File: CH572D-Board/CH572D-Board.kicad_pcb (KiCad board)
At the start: 2 copper layers, 16.4 x 26.4 mm, 17 parts, among them J1 12402012E212A, J2 Conn_PinHeader_1x07_P2.54mm_V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, U2 MIC5504-3.3YM5-TR, Y1 32mhz

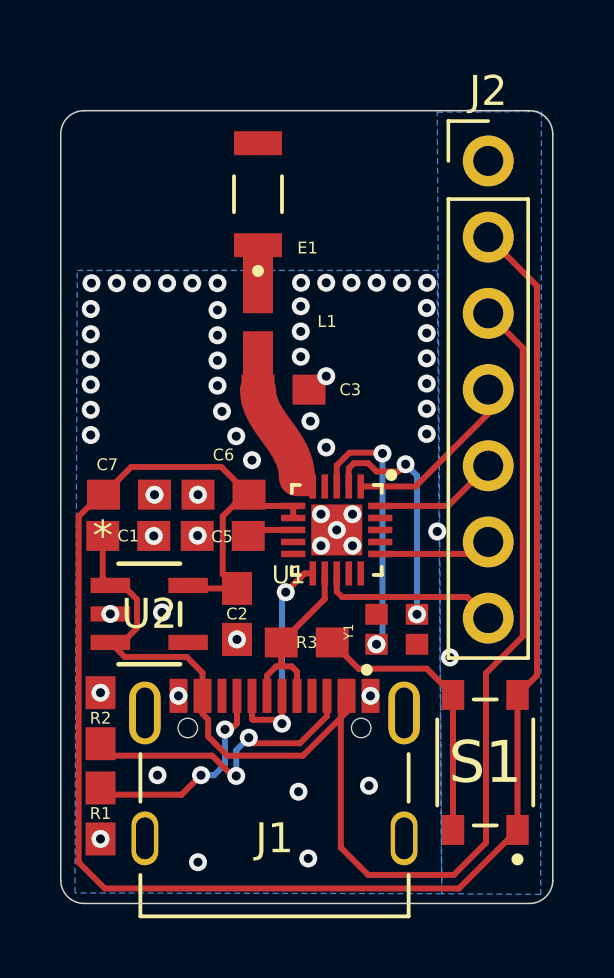
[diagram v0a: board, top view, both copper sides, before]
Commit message: fixed 5v
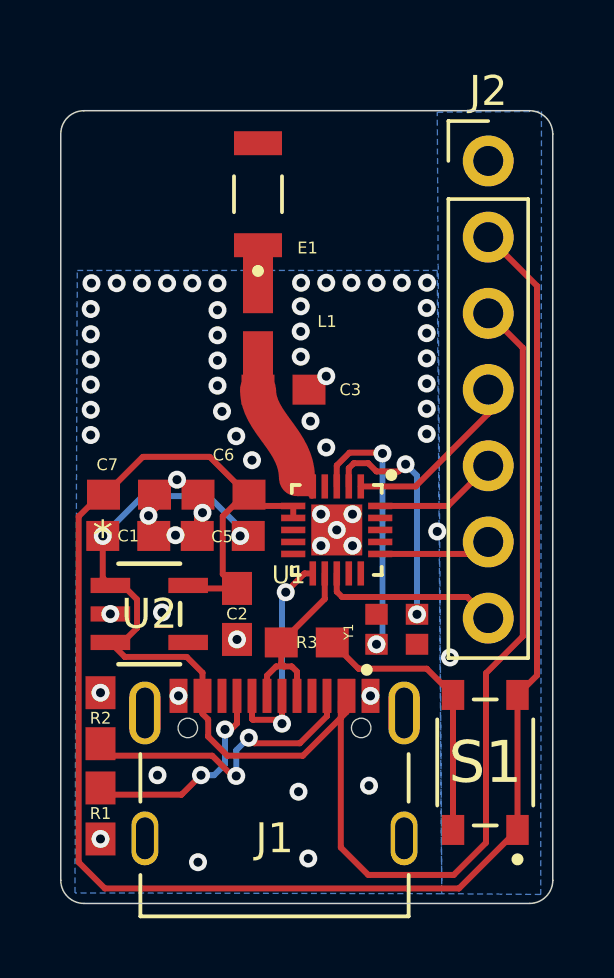
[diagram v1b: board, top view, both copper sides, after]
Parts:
- C1: value 1uF -> 0.1uF
- U2: value MIC5504-3.3YM5-TR -> the really cheap one (200mah)
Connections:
- C5 pad 1: V5 -> +5V
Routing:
- net +5V: track 46.0 -> 51.9 mm, vias 0 -> 2
- net GND: track 0.07 -> 2.55 mm
- net V5: track 1.58 -> 0.00 mm
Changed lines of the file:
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@@
 			)
 		)
-		(property "Value" "MIC5504-3.3YM5-TR"
+		(property "Value" "the really cheap one (200mah)"
 			(at 0 0 0)
 			(unlocked yes)
@@
 			(size 1.1 1)
 			(layers "F.Cu" "F.Mask" "F.Paste")
-			(net 11 "V5")
+			(net 1 "+5V")
 			(pintype "passive")
 			(solder_mask_margin 0.102)
@@
 			)
 		)
-		(property "Value" "1uF"
+		(property "Value" "0.1uF"
 			(at 1.34 1.27 0)
 			(layer "F.Fab")
@@
 		(net 1)
 	)
+	(via
+		(at 154.525 133.775)
+		(size 0.6)
+		(drill 0.3)
+		(layers "F.Cu" "B.Cu")
+		(net 1)
+	)
+	(via
+		(at 159.107 133.775)
+		(size 0.6)
+		(drill 0.3)
+		(layers "F.Cu" "B.Cu")
+		(net 1)
+	)
 	(segment
-		(start 157.6875 133.7625)
-		(end 157.675 133.775)
+		(start 155.854 132.446)
+		(end 158.046 132.446)
 		(width 0.2)
-		(layer "F.Cu")
-		(net 2)
+		(layer "B.Cu")
+		(net 1)
+	)
+	(segment
+		(start 159.107 133.507)
+		(end 159.107 133.775)
+		(width 0.2)
+		(layer "B.Cu")
+		(net 1)
+	)
+	(segment
+		(start 154.525 133.775)
+		(end 155.854 132.446)
+		(width 0.2)
+		(layer "B.Cu")
+		(net 1)
+	)
+	(segment
+		(start 158.046 132.446)
+		(end 159.107 133.507)
+		(width 0.2)
+		(layer "B.Cu")
+		(net 1)
 	)
 	(segment
 		(start 156.225 132.425)
-		(end 156.25 132.4)
+		(end 156.3 132.5)
 		(width 0.2)
 		(layer "F.Cu")
@@
 	(segment
 		(start 157.7 133.75)
-		(end 157.6875 133.7625)
+		(end 157.675002 133.725002)
+		(width 0.2)
+		(layer "F.Cu")
+		(net 2)
+	)
+	(segment
+		(start 157.75 133)
+		(end 157.85 133)
+		(width 0.2)
+		(layer "F.Cu")
+		(net 2)
+	)
+	(segment
+		(start 157.675 133.775)
+		(end 157.675 133.075)
+		(width 0.2)
+		(layer "F.Cu")
+		(net 2)
+	)
+	(segment
+		(start 157.675 133.075)
+		(end 157.75 133)
+		(width 0.2)
+		(layer "F.Cu")
+		(net 2)
+	)
+	(segment
+		(start 156.3 132.85)
+		(end 156.05 133.1)
+		(width 0.2)
+		(layer "F.Cu")
+		(net 2)
+	)
+	(segment
+		(start 157.675002 133.725002)
+		(end 157.675002 133.174998)
+		(width 0.2)
+		(layer "F.Cu")
+		(net 2)
+	)
+	(segment
+		(start 156.3 132.5)
+		(end 156.3 132.85)
+		(width 0.2)
+		(layer "F.Cu")
+		(net 2)
+	)
+	(segment
+		(start 157.675002 133.174998)
+		(end 157.85 133)
 		(width 0.2)
 		(layer "F.Cu")
@@
 	)
 	(via
-		(at 157.6875 133.7625)
+		(at 157.85 133)
 		(size 0.6)
 		(drill 0.3)
@@
 	)
 	(via
-		(at 156.225 133.775)
+		(at 156.95 133.75)
 		(size 0.6)
 		(drill 0.3)
@@
 	)
 	(via
-		(at 156.25 132.4)
+		(at 156.05 133.1)
 		(size 0.6)
 		(drill 0.3)
@@
 	)
 	(via
-		(at 157.7 132.4)
+		(at 157 131.9)
 		(size 0.6)
 		(drill 0.3)
@@
 	)
 	(segment
+		(start 159.35 132.4)
+		(end 159.4 132.4)
+		(width 0.2)
+		(layer "F.Cu")
+		(net 3)
+	)
+	(segment
 		(start 169 125.44)
 		(end 169 138.425)
@@
 	)
 	(segment
-		(start 159 135.525)
-		(end 158.525 135.05)
+		(start 160.875 133.175)
+		(end 160.875 132.775)
 		(width 0.2)
 		(layer "F.Cu")
@@
 	)
 	(segment
-		(start 160.875 133.175)
-		(end 160.875 132.775)
+		(start 153.722 133.125)
+		(end 154.447 132.4)
 		(width 0.2)
 		(layer "F.Cu")
@@
 	)
 	(segment
-		(start 158.475 131.475)
-		(end 159.4 132.4)
+		(start 159.244 132.4)
+		(end 159.8 132.4)
 		(width 0.2)
 		(layer "F.Cu")
@@
 	)
 	(segment
-		(start 153.722 133.125)
-		(end 154.447 132.4)
+		(start 159 135.525)
+		(end 158.525 135.05)
 		(width 0.2)
 		(layer "F.Cu")
@@
 	)
 	(segment
-		(start 154.55 132.4)
-		(end 155.475 131.475)
+		(start 168.35 143.575)
+		(end 168.35 139.075)
 		(width 0.2)
 		(layer "F.Cu")
@@
 	)
 	(segment
-		(start 158.525 133.119)
-		(end 159.244 132.4)
+		(start 153.722 144.653)
+		(end 153.722 133.125)
 		(width 0.2)
 		(layer "F.Cu")
@@
 	)
 	(segment
-		(start 168.35 143.575)
-		(end 168.35 139.075)
+		(start 155.862 131.138)
+		(end 158.088 131.138)
 		(width 0.2)
 		(layer "F.Cu")
@@
 	)
 	(segment
-		(start 153.722 144.653)
-		(end 153.722 133.125)
+		(start 154.6 132.4)
+		(end 155.862 131.138)
 		(width 0.2)
 		(layer "F.Cu")
@@
 	)
 	(segment
-		(start 155.475 131.475)
-		(end 158.475 131.475)
+		(start 158.525 133.119)
+		(end 159.244 132.4)
+		(width 0.2)
+		(layer "F.Cu")
+		(net 3)
+	)
+	(segment
+		(start 158.525 135.05)
+		(end 158.525 133.119)
 		(width 0.2)
 		(layer "F.Cu")
@@
 	)
 	(segment
-		(start 158.525 135.05)
-		(end 158.525 133.119)
-		(width 0.2)
-		(layer "F.Cu")
-		(net 3)
-	)
-	(segment
 		(start 154.594 145.525)
 		(end 153.722 144.653)
@@
 	)
 	(segment
-		(start 159.244 132.4)
-		(end 159.8 132.4)
+		(start 158.088 131.138)
+		(end 159.35 132.4)
 		(width 0.2)
 		(layer "F.Cu")
@@
 	)
 	(segment
+		(start 154.55 132.4)
+		(end 154.6 132.4)
+		(width 0.2)
+		(layer "F.Cu")
+		(net 3)
+	)
+	(segment
 		(start 160.304 138.125)
 		(end 160 138.429)
@@
 	)
 	(segment
-		(start 159.375 133.775)
-		(end 159.575 133.575)
-		(width 0.2)
-		(layer "F.Cu")
-		(net 11)
-	)
-	(segment
-		(start 159.575 133.575)
-		(end 160.875 133.575)
-		(width 0.2)
-		(layer "F.Cu")
-		(net 11)
-	)
-	(segment
